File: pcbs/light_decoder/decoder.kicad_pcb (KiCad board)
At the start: 2 copper layers, 77.7 x 45.7 mm, 29 parts, among them J1 Screw_Terminal_01x08, J2 AVR-ISP-6, J3 Screw_Terminal_01x08, J4 RJ45_LED_Shielded, J5 RJ45_LED_Shielded, J6 Screw_Terminal_01x01, Q13 2N7002, SW1 SW_DIP_x06, U1 ATmega328P-AU, U10 74HC595, U2 74HC595, U4 MAX481E, Y1 16MHz

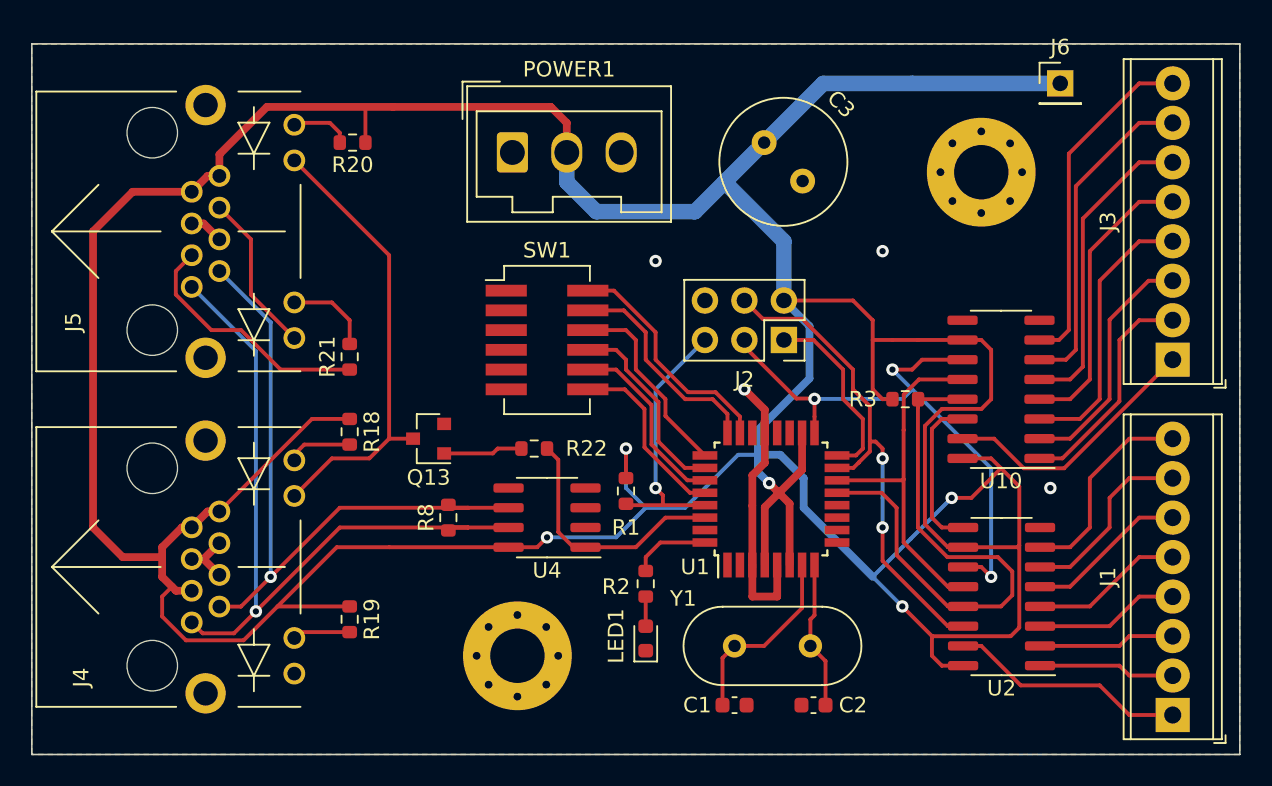
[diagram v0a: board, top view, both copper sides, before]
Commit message: produced PCBs, dropped baudrate, removed on-board dynamic address selection - decoder must now be configured via programmer!
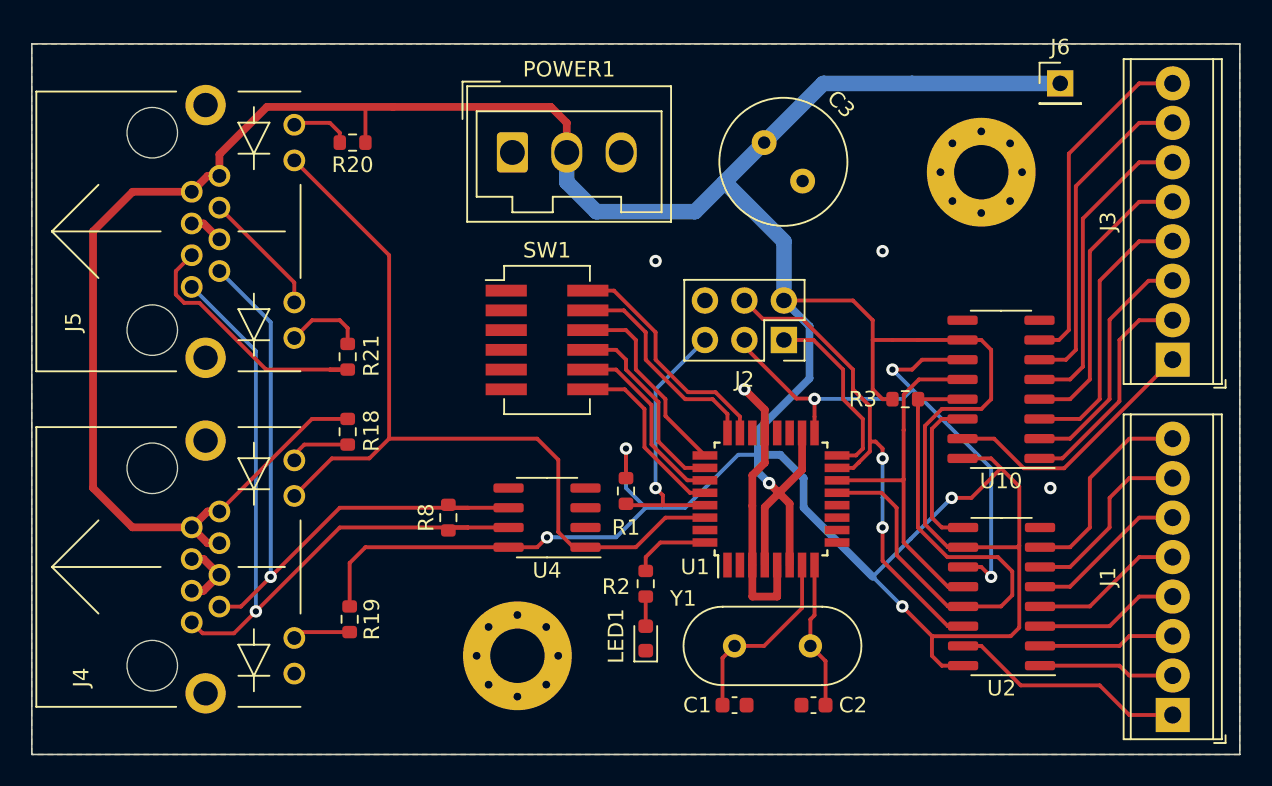
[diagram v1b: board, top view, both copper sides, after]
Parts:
- removed Q13: 2N7002, Package_TO_SOT_SMD:SOT-23
- removed R22: 1k, Resistor_SMD:R_0603_1608Metric
- moved R21 0.13 mm to (113.5, 88.1)
- moved R18 0.13 mm to (113.5, 92.9)
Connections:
- net /networking/A+ renamed Net-(J4-Pad1)
- net /networking/A- renamed Net-(J4-Pad2)
- J4 pad 11: Net-(J4-Pad11) -> /networking/Rx
- J4 pad 3: 5V -> GND
- J4 pad 6: GND -> 5V
- J5 pad 11: Net-(J4-Pad11) -> /networking/Rx
- J5 pad 6: Net-(J5-Pad6) -> Net-(J5-Pad10)
- J5 pad 9: Net-(J5-Pad6) -> Net-(J5-Pad9)
- R21 pad 2: Net-(J5-Pad10) -> Net-(J5-Pad9)
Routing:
- net /networking/Rx: track 16.3 -> 54.8 mm
- net Net-(J4-Pad11): track 29.6 -> 0.00 mm
- net 5V: track 310.8 -> 287.3 mm
- net Net-(J5-Pad6): track 10.4 -> 0.00 mm
- net Net-(J5-Pad9): track 0.00 -> 5.13 mm
- net Net-(Q13-Pad1): track 5.10 -> 0.00 mm
- net Net-(J5-Pad10): track 5.56 -> 8.10 mm
- net GND: track 23.9 -> 24.6 mm
- net Net-(J5-Pad3): track 16.1 -> 16.6 mm
